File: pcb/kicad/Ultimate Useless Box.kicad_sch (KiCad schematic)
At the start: 14 parts, among them J1 POWER_FROM_TP4056, J2 5V_BOOST_MODULE, U1 ESP32-S3-DevKitC, U2 DRV8833PWP

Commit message: add GPIO headers, wire sensor
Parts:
- removed J_TOF: VL53L0X_Up, symbol Connector_Generic:Conn_01x05
- added J3: Conn_01x10_Pin, symbol Connector:Conn_01x10_Pin
- added J_TOF: VL53L0X, symbol Connector_Generic:Conn_01x06
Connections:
- net +3.3V: now also J3.10 (Pin_10), J_TOF.1 (Pin_1)
- net +5V: now also J3.9 (Pin_9)
- net GND: now also J3.7 (Pin_7), J3.8 (Pin_8), J_TOF.2 (Pin_2)
- net SCL: now also U1.41 (GPIO1/ADC1_CH0), J_TOF.4 (Pin_4)
- net SDA: now also U1.31 (GPIO0), J_TOF.3 (Pin_3)
- net SERVO2_SIG: now also U1.12 (GPIO8/ADC1_CH7); no longer U1.13 (GPIO3/ADC1_CH2)
- new net TOF_INT: J_TOF.5 (Pin_5)
- new net TOF_SHUT: J_TOF.6 (Pin_6)
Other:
- note added: "Expansion Header - Extra GPIO and Power In case I need something else"
- moved on the sheet: J_OLED

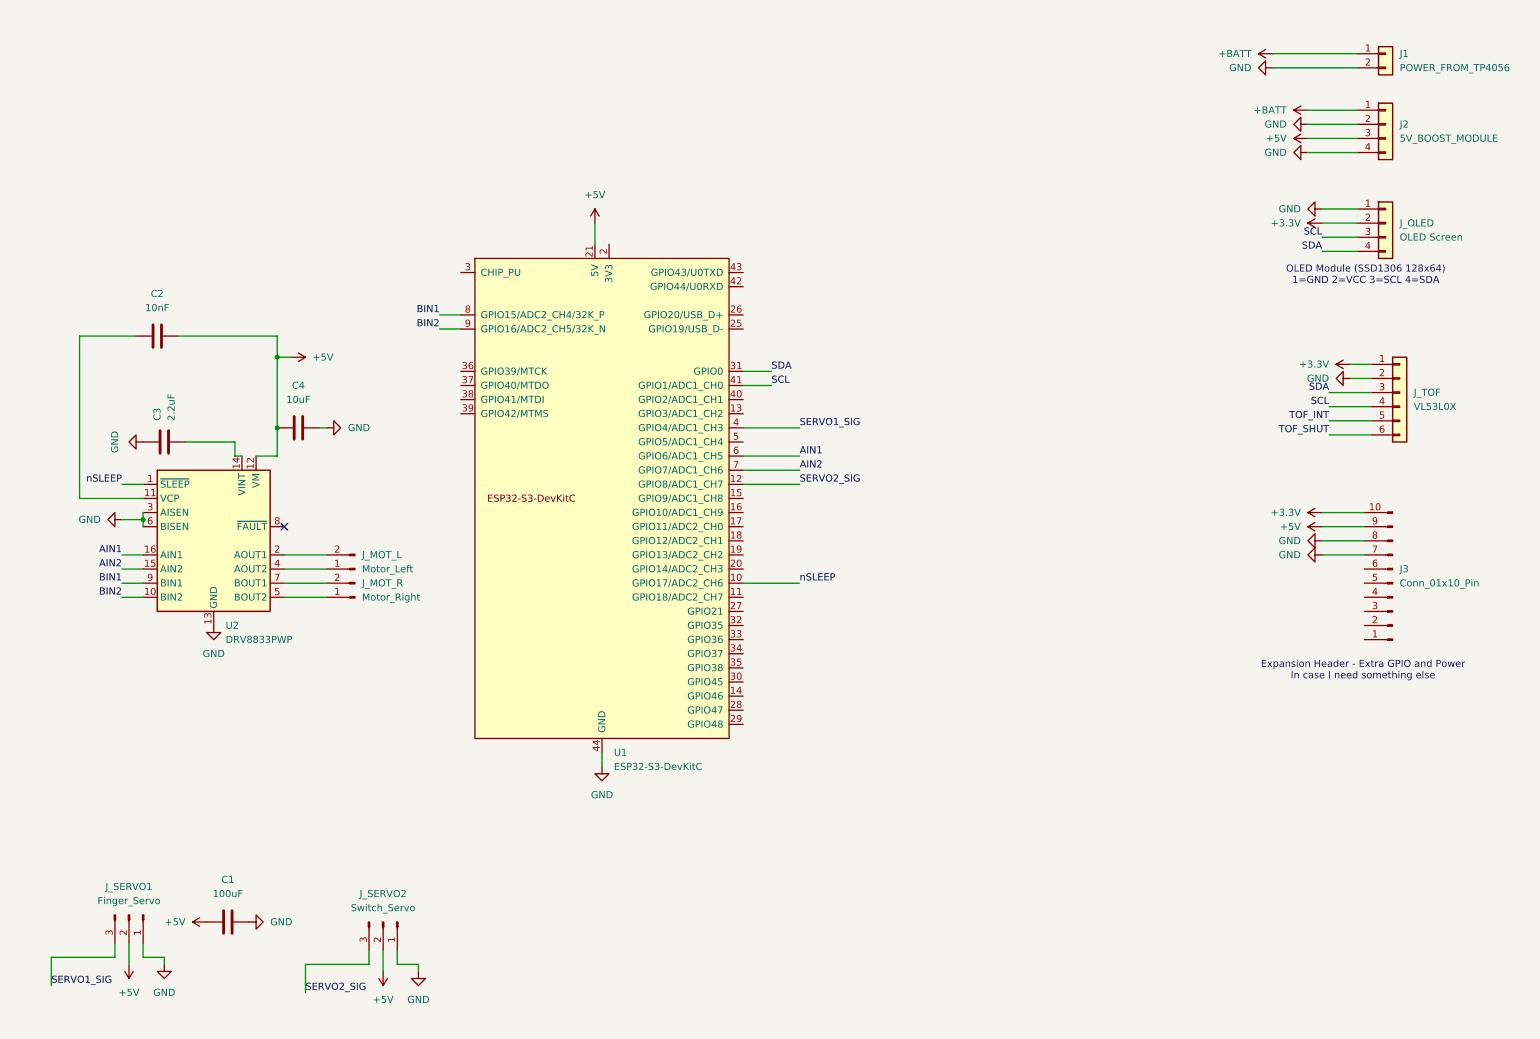
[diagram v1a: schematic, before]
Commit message: Finish schematic
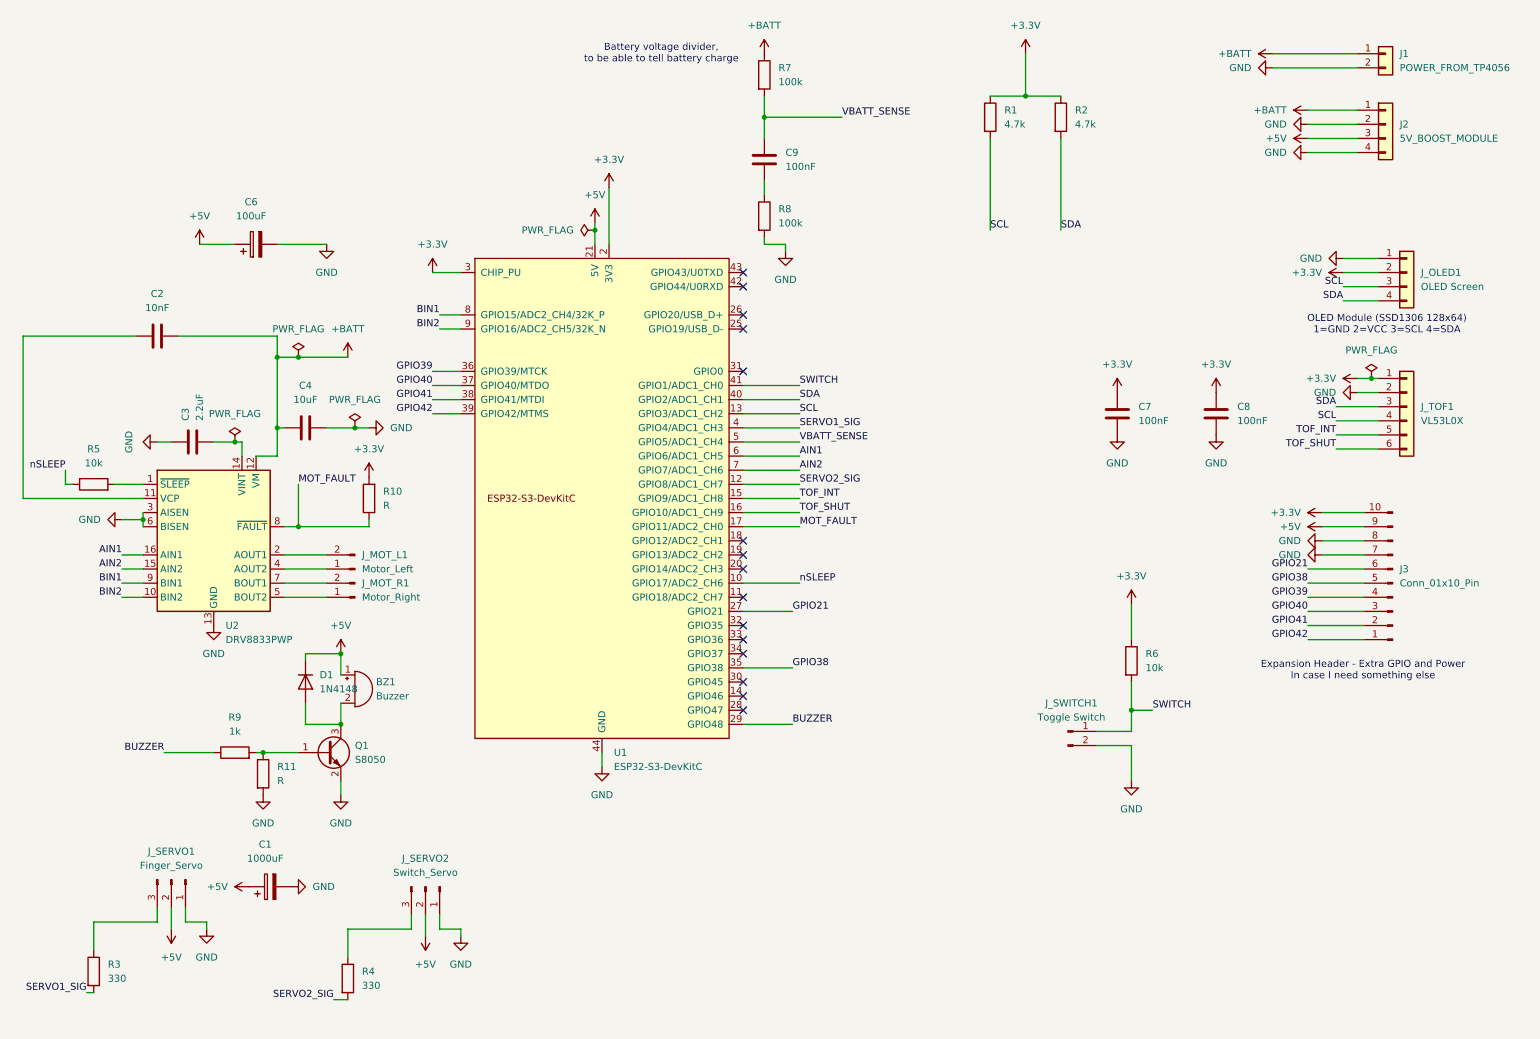
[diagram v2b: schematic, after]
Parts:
- removed C1: 100uF, symbol Device:C
- added BZ1: Buzzer, symbol Device:Buzzer
- added C1: 1000uF, symbol Device:C_Polarized
- added C6: 100uF, symbol Device:C_Polarized
- added C7, C8, C9: 100nF, symbol Device:C
- added D1: 1N4148, symbol Device:D
- added J_SWITCH1: Toggle Switch, symbol Connector:Conn_01x02_Pin
- added Q1: S8050, symbol Transistor_BJT:Q_NPN_BEC
- added R1, R2: 4.7k, symbol Device:R
- added R10, R11: R, symbol Device:R
- added R3, R4: 330, symbol Device:R
- added R5, R6: 10k, symbol Device:R
- added R7, R8: 100k, symbol Device:R
- added R9: 1k, symbol Device:R
- renumbered J_MOT_L to J_MOT_L1, J_MOT_R to J_MOT_R1, J_OLED to J_OLED1, J_TOF to J_TOF1
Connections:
- net +3.3V: now also U1.1 (3V3), U1.2 (3V3), U1.3 (CHIP_PU), C7.1, C8.1, R1.1, R10.2, R2.1, R6.1
- net +5V: now also BZ1.1 (+), C1.1, C6.1, D1.1 (K); no longer C2.2, C4.1, U2.12 (VM)
- net +BATT: now also C2.2, C4.1, U2.12 (VM), R7.1
- net GND: now also C1.2, C6.2, C7.2, C8.2, J_SWITCH1.2 (Pin_2), Q1.2 (E), R11.2, R8.2
- net SCL: now also U1.13 (GPIO3/ADC1_CH2), R1.2; no longer U1.41 (GPIO1/ADC1_CH0)
- net SDA: now also U1.40 (GPIO2/ADC1_CH1), R2.2; no longer U1.31 (GPIO0)
- net SERVO1_SIG: now also R3.2; no longer J_SERVO1.3 (Pin_3)
- net SERVO2_SIG: now also R4.2; no longer J_SERVO2.3 (Pin_3)
- net TOF_INT: now also U1.15 (GPIO9/ADC1_CH8)
- net TOF_SHUT: now also U1.16 (GPIO10/ADC1_CH9)
- net nSLEEP: now also R5.1; no longer U2.1 (~{SLEEP})
- net MOT_FAULT: now reaches U2.8 (~{FAULT})
- net MOT_FAULT: now also U1.17 (GPIO11/ADC2_CH0), R10.1
- net GPIO42: now reaches J3.1 (Pin_1)
- net GPIO42: now also U1.39 (GPIO42/MTMS)
- net GPIO41: now reaches J3.2 (Pin_2)
- net GPIO41: now also U1.38 (GPIO41/MTDI)
- net GPIO40: now reaches J3.3 (Pin_3)
- net GPIO40: now also U1.37 (GPIO40/MTDO)
- net GPIO39: now reaches J3.4 (Pin_4)
- net GPIO39: now also U1.36 (GPIO39/MTCK)
- net GPIO38: now reaches J3.5 (Pin_5)
- net GPIO38: now also U1.35 (GPIO38)
- net GPIO21: now reaches J3.6 (Pin_6)
- net GPIO21: now also U1.27 (GPIO21)
- net BUZZER: now reaches U1.29 (GPIO48)
- net BUZZER: now also R9.1
- net VBATT_SENSE: now reaches U1.5 (GPIO5/ADC1_CH4)
- net VBATT_SENSE: now also C9.1, R7.2
- new net: R5.2, U2.1 (~{SLEEP})
- new net: J_SERVO2.3 (Pin_3), R4.1
- new net: J_SERVO1.3 (Pin_3), R3.1
- new net: C9.2, R8.1
- new net: Q1.1 (B), R11.1, R9.2
- new net: BZ1.2 (-), D1.2 (A), Q1.3 (C)
- new net SWITCH: J_SWITCH1.1 (Pin_1), R6.2, U1.41 (GPIO1/ADC1_CH0)
- no-connect marks 1 -> 15
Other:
- note added: "Battery voltage divider, to be able to tell battery charge"
- moved on the sheet: C3, C4, J_OLED1, J_SERVO1, J_SERVO2, J_TOF1

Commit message: Finish Kicad
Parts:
- removed J1: POWER_FROM_TP4056, symbol Connector_Generic:Conn_01x02
- removed J2: 5V_BOOST_MODULE, symbol Connector_Generic:Conn_01x04
- added C10, C5: 10uF, Capacitor_SMD:C_0805_2012Metric, symbol Device:C
- added C11, C12: 22uF, Capacitor_SMD:C_0805_2012Metric, symbol Device:C
- added D2: LED, LED_THT:LED_D5.0mm, symbol Device:LED
- added D3: D, Diode_SMD:D_SMA, symbol Device:D
- added J1: USB_C_Receptacle_USB2.0_16P, Connector_USB:USB_C_Receptacle_HRO_TYPE-C-31-M-12, symbol Connector:USB_C_Receptacle_USB2.0_16P
- added J_BATT1: Conn_01x02_Pin, Connector_JST:JST_PH_B2B-PH-K_1x02_P2.00mm_Vertical, symbol Connector:Conn_01x02_Pin
- added L1: 4.7uH, Inductor_SMD:L_Taiyo-Yuden_NR-40xx, symbol Device:L
- added R12: 1k, Resistor_SMD:R_0805_2012Metric, symbol Device:R
- added R13: 1.2k, Resistor_SMD:R_0805_2012Metric, symbol Device:R
- added R14: 110k, Resistor_SMD:R_0805_2012Metric, symbol Device:R
- added R15: 15k, Resistor_SMD:R_0805_2012Metric, symbol Device:R
- added R16, R17: 5.1k, Resistor_SMD:R_0805_2012Metric, symbol Device:R
- added U3: TP4056-42-ESOP8, Package_SO:SOIC-8-1EP_3.9x4.9mm_P1.27mm_EP2.41x3.3mm_ThermalVias, symbol Battery_Management:TP4056-42-ESOP8
- added U4: MT3608, Package_TO_SOT_SMD:SOT-23-6, symbol Regulator_Switching:MT3608
- BZ1: footprint (none) -> Buzzer_Beeper:Buzzer_12x9.5RM7.6
- C1: value 1000uF -> 100uF; footprint (none) -> Capacitor_THT:CP_Radial_D8.0mm_P3.50mm
- C2, C3, C4, C7, C8, C9: footprint (none) -> Capacitor_SMD:C_0805_2012Metric
- C6: footprint (none) -> Capacitor_THT:CP_Radial_D8.0mm_P3.50mm
- D1: footprint (none) -> Diode_SMD:D_SOD-323
- J3: footprint (none) -> Connector_PinHeader_2.54mm:PinHeader_1x10_P2.54mm_Vertical
- J_MOT_L1, J_MOT_R1, J_SWITCH1: footprint (none) -> Connector_JST:JST_PH_B2B-PH-K_1x02_P2.00mm_Vertical
- J_OLED1: footprint (none) -> Connector_JST:JST_PH_B4B-PH-K_1x04_P2.00mm_Vertical
- J_SERVO1, J_SERVO2: footprint (none) -> Connector_PinHeader_2.54mm:PinHeader_1x03_P2.54mm_Vertical
- J_TOF1: footprint (none) -> Connector_JST:JST_PH_B6B-PH-K_1x06_P2.00mm_Vertical
- Q1: footprint (none) -> Package_TO_SOT_SMD:SOT-23
- R1, R2, R3, R4, R5, R6, R7, R8, R9: footprint (none) -> Resistor_SMD:R_0805_2012Metric
- R10, R11: value R -> 10k; footprint (none) -> Resistor_SMD:R_0805_2012Metric
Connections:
- net +3.3V: no longer U1.3 (CHIP_PU)
- net +5V: now also C12.1, D3.1 (K), R14.1
- net +BATT: now also C10.1, C11.1, J_BATT1.1 (Pin_1), L1.1, U3.5 (BAT), U4.5 (IN)
- net SCL: now also U1.18 (GPIO12/ADC2_CH1); no longer U1.13 (GPIO3/ADC1_CH2)
- net GND renamed -BATT
- net -BATT: now also C10.2, C11.2, C12.2, C5.1, J1.A1 (GND), J1.A12 (GND), J1.B1 (GND), J1.B12 (GND), J1.S1 (SHIELD), J_BATT1.2 (Pin_2), R13.2, R15.2, R16.2, R17.2, U3.1 (TEMP), U3.3 (GND), U3.9 (EPAD), U4.2 (GND), U4.4 (EN)
- new net: D3.2 (A), L1.2, U4.1 (SW)
- new net: R14.2, R15.1, U4.3 (FB)
- new net: D2.1 (K), R12.1
- new net: R12.2, U3.7 (~{CHRG})
- new net: R13.1, U3.2 (PROG)
- new net: J1.B5 (CC2), R17.1
- new net: J1.A5 (CC1), R16.1
- new net VBUS: C5.2, D2.2 (A), J1.A4 (VBUS), J1.A9 (VBUS), J1.B4 (VBUS), J1.B9 (VBUS), U3.4 (V_{CC}), U3.8 (CE)
- no-connect marks 15 -> 23
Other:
- moved on the sheet: C7, C8, J3, J_OLED1, J_SWITCH1, J_TOF1, R6
